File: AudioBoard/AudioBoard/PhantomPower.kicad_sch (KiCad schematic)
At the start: 0 parts

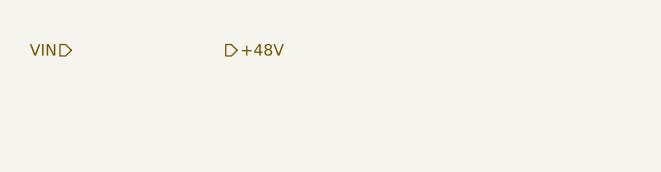
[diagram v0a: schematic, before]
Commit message: added pwr sw and headphone out
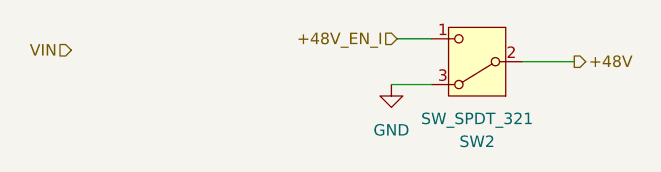
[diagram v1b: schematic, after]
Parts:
- added SW2: SW_SPDT_321, haoyu:SS-12D28G7, symbol Switch:SW_SPDT_321
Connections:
- net +48V: now also SW2.2 (B)
- new net +48V_EN_I: SW2.1 (C)
- new net GND: SW2.3 (A)
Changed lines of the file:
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@@
 	(generator_version "10.0")
 	(paper "A4")
+	(wire
+		(pts
+			(xy 101.6 61.595) (xy 95.885 61.595)
+		)
+		(stroke
+			(width 0)
+			(type default)
+		)
+	)
+	(wire
+		(pts
+			(xy 81.28 64.135) (xy 85.725 64.135)
+		)
+		(stroke
+			(width 0)
+			(type default)
+		)
+	)
+	(wire
+		(pts
+			(xy 81.915 59.055) (xy 85.725 59.055)
+		)
+		(stroke
+			(width 0)
+			(type default)
+		)
+	)
+	(hierarchical_label "+48V_EN_I"
+		(shape input)
+		(at 81.915 59.055 180)
+		(effects
+			(font
+				(size 1.27 1.27)
+			)
+			(justify right)
+		)
+	)
 	(hierarchical_label "+48V"
 		(shape output)
-		(at 62.865 60.325 0)
+		(at 101.6 61.595 0)
 		(effects
 			(font
@@
 		)
 	)
+	(symbol
+		(lib_id "Switch:SW_SPDT_321")
+		(at 90.805 61.595 180)
+		(unit 1)
+		(body_style 1)
+		(exclude_from_sim no)
+		(in_bom yes)
+		(on_board yes)
+		(in_pos_files yes)
+		(dnp no)
+		(fields_autoplaced yes)
+		(property "Reference" "SW2"
+			(at 90.805 70.485 0)
+			(show_name no)
+			(do_not_autoplace no)
+			(effects
+				(font
+					(size 1.27 1.27)
+				)
+			)
+		)
+		(property "Value" "SW_SPDT_321"
+			(at 90.805 67.945 0)
+			(show_name no)
+			(do_not_autoplace no)
+			(effects
+				(font
+					(size 1.27 1.27)
+				)
+			)
+		)
+		(property "Footprint" "haoyu:SS-12D28G7"
+			(at 90.805 51.435 0)
+			(hide yes)
+			(show_name no)
+			(do_not_autoplace no)
+			(effects
+				(font
+					(size 1.27 1.27)
+				)
+			)
+		)
+		(property "Datasheet" ""
+			(at 90.805 53.975 0)
+			(hide yes)
+			(show_name no)
+			(do_not_autoplace no)
+			(effects
+				(font
+					(size 1.27 1.27)
+				)
+			)
+		)
+		(property "Description" "Switch, single pole double throw"
+			(at 90.805 61.595 0)
+			(hide yes)
+			(show_name no)
+			(do_not_autoplace no)
+			(effects
+				(font
+					(size 1.27 1.27)
+				)
+			)
+		)
+		(property "jlcpcbpart" "C2884748"
+			(at 90.805 61.595 0)
+			(hide yes)
+			(show_name no)
+			(do_not_autoplace no)
+			(effects
+				(font
+					(size 1.27 1.27)
+				)
+			)
+		)
+		(pin "3"
+		)
+		(pin "1"
+		)
+		(pin "2"
+		)
+		(instances
+			(project "AudioBoard"
+				(path "/dd5d876d-fff7-4cb4-baee-a023036d12ae/ee404ad0-726e-426f-8607-a7730f1919f6/1be5cbb9-85cd-45d8-b0f1-73b7fc7bb211"
+					(reference "SW2")
+					(unit 1)
+				)
+			)
+		)
+	)
+	(symbol
+		(lib_id "power:GND")
+		(at 81.28 64.135 0)
+		(unit 1)
+		(body_style 1)
+		(exclude_from_sim no)
+		(in_bom yes)
+		(on_board yes)
+		(in_pos_files yes)
+		(dnp no)
+		(fields_autoplaced yes)
+		(property "Reference" "#PWR088"
+			(at 81.28 70.485 0)
+			(hide yes)
+			(show_name no)
+			(do_not_autoplace no)
+			(effects
+				(font
+					(size 1.27 1.27)
+				)
+			)
+		)
+		(property "Value" "GND"
+			(at 81.28 69.215 0)
+			(show_name no)
+			(do_not_autoplace no)
+			(effects
+				(font
+					(size 1.27 1.27)
+				)
+			)
+		)
+		(property "Footprint" ""
+			(at 81.28 64.135 0)
+			(hide yes)
+			(show_name no)
+			(do_not_autoplace no)
+			(effects
+				(font
+					(size 1.27 1.27)
+				)
+			)
+		)
+		(property "Datasheet" ""
+			(at 81.28 64.135 0)
+			(hide yes)
+			(show_name no)
+			(do_not_autoplace no)
+			(effects
+				(font
+					(size 1.27 1.27)
+				)
+			)
+		)
+		(property "Description" ""
+			(at 81.28 64.135 0)
+			(show_name no)
+			(do_not_autoplace no)
+			(effects
+				(font
+					(size 1.27 1.27)
+				)
+			)
+		)
+		(pin "1"
+		)
+		(instances
+			(project "AudioBoard"
+				(path "/dd5d876d-fff7-4cb4-baee-a023036d12ae/ee404ad0-726e-426f-8607-a7730f1919f6/1be5cbb9-85cd-45d8-b0f1-73b7fc7bb211"
+					(reference "#PWR088")
+					(unit 1)
+				)
+			)
+		)
+	)

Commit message: added lcscpart to components and assigned footprints
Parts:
- SW2: JLCPCB (none) -> C2884748; LCSC Part (none) -> C2884748
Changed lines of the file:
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@@
+			)
+		)
+		(property "JLCPCB" "C2884748"
+			(at 90.805 61.595 0)
+			(hide yes)
+			(show_name no)
+			(do_not_autoplace no)
+			(effects
+				(font
+					(size 1.27 1.27)
+				)
+			)
+		)
+		(property "LCSC Part" "C2884748"
+			(at 90.805 61.595 0)
+			(hide yes)
+			(show_name no)
+			(do_not_autoplace no)
+			(effects
+				(font
+					(size 1.27 1.27)
+				)
 			)
 		)
